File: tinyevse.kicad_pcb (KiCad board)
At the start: 2 copper layers, 76.2 x 50.8 mm, 26 parts, among them IC1 ATMEGA328P-P, P1 SERIAL, P2 12V input, P3 ICSP, P4 Pilot, SW1 RESET_BUTTON, U1 7805, U2 IXDD604PI, X1 16MHz

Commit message: add 2-pin connector for external relay coil
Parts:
- added P5: RELAYCOIL, battery-dlg:CCFLHV, F.Cu at (81.4, 72.2)
- D1: value D -> 1N4007
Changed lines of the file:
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@@
 (kicad_pcb (version 4) (host pcbnew 4.0.2-4+6225~38~ubuntu14.04.1-stable)
   (general
-    (links 58)
-    (no_connects 58)
-    (area 22.66 22.066365 101.675001 76.275001)
+    (links 60)
+    (no_connects 60)
+    (area 22.66 22.066365 101.675001 91.302452)
     (thickness 1.6)
     (drawings 4)
     (tracks 0)
     (zones 0)
-    (modules 26)
+    (modules 27)
     (nets 40)
   )
@@
       (effects (font (size 1 1) (thickness 0.15)))
     )
-    (fp_text value D (at 4.37134 -3.55854 180) (layer F.Fab)
+    (fp_text value 1N4007 (at 4.37134 -3.55854 180) (layer F.Fab)
       (effects (font (size 1 1) (thickness 0.15)))
     )
@@
       (scale (xyz 1 1 1))
       (rotate (xyz 0 0 0))
+    )
+  )
+  (module battery-dlg:CCFLHV (layer F.Cu)
+    (at 81.41 72.25 180)
+    (descr "Bornier d'alimentation 2 pins")
+    (tags DEV)
+    (fp_text reference P5 (at 0 -5.08 180) (layer F.SilkS)
+      (effects (font (thickness 0.3048)))
+    )
+    (fp_text value RELAYCOIL (at 6.36016 -1.23952 270) (layer F.SilkS)
+      (effects (font (thickness 0.3048)))
+    )
+    (fp_line (start 5.08 2.54) (end -5.08 2.54) (layer F.SilkS) (width 0.3048))
+    (fp_line (start 5.08 2.54) (end 5.08 -3.81) (layer F.SilkS) (width 0.3048))
+    (fp_line (start 5.08 -3.81) (end -5.08 -3.81) (layer F.SilkS) (width 0.3048))
+    (fp_line (start -5.08 -3.81) (end -5.08 2.54) (layer F.SilkS) (width 0.3048))
+    (pad 1 thru_hole rect (at -2.54 0 180) (size 2.54 2.54) (drill 1.524) (layers *.Cu *.Mask F.SilkS)
+      (net 8 /RELAY_COIL))
+    (pad 2 thru_hole circle (at 2.54 0 180) (size 2.54 2.54) (drill 1.524) (layers *.Cu *.Mask F.SilkS)
+      (net 4 GND))
+    (model device/bornier_2.wrl
+      (at (xyz 0 0 0))
+      (scale (xyz 1 1 1))
+      (rotate (xyz 0 0 0))

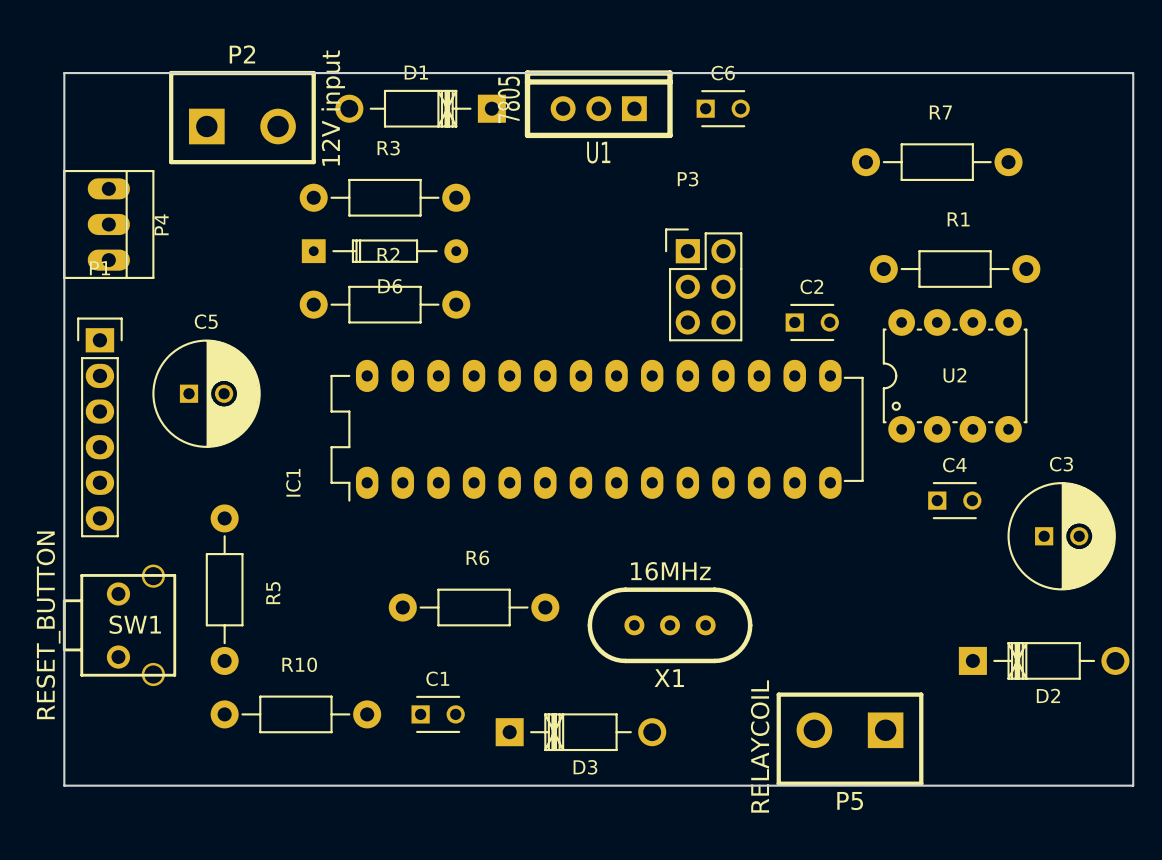
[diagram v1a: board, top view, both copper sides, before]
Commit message: switch driver chip to make bipolar pilot signal
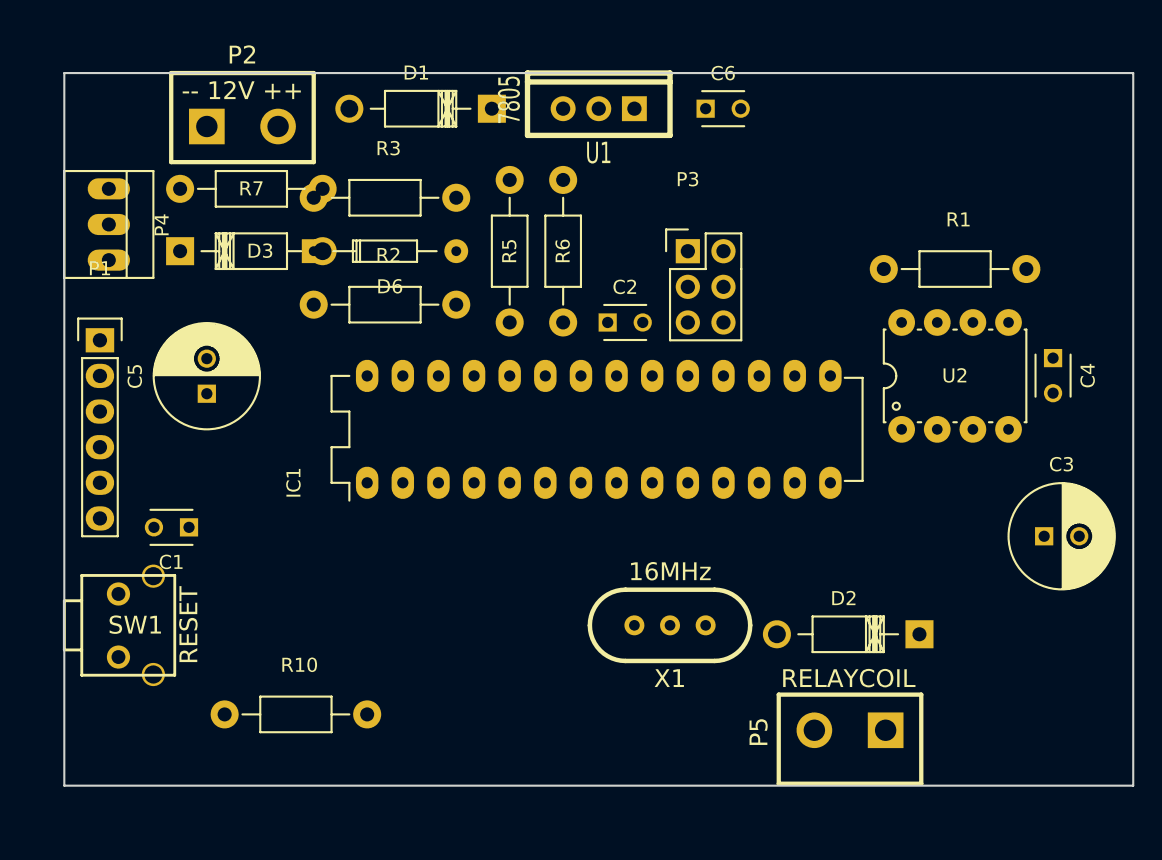
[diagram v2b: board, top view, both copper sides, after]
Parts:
- P2: value 12V input -> -- 12V ++
- SW1: value RESET_BUTTON -> RESET
- moved R7 48.9 mm to (33.7, 33.7)
- moved D3 41.6 mm to (33.7, 38.1)
- moved R5 31.5 mm to (57.1, 33.0)
- moved R6 23.3 mm to (61.0, 43.2), turned to 90 degrees
- moved C1 21.2 mm to (34.3, 57.8), turned to 180 degrees
- moved C2 13.3 mm to (64.1, 43.2)
- moved C4 13.1 mm to (95.9, 45.7), turned to 270 degrees
- moved D2 4.26 mm to (86.4, 65.4), turned to 180 degrees
- moved C5 1.27 mm to (35.6, 48.3), turned to 90 degrees
